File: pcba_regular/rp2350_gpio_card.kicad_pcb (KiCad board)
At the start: 4 copper layers, 26 x 30 mm, 37 parts, among them J1 Conn_01x10_Pin, J2 Conn_01x10_Pin, P1 USB_C_Plug_USB2.0, U1 RP2350_60QFN, U2 W25Q128JVS, U4 AP2127K-3.3, Y1 ABM8-272-T3

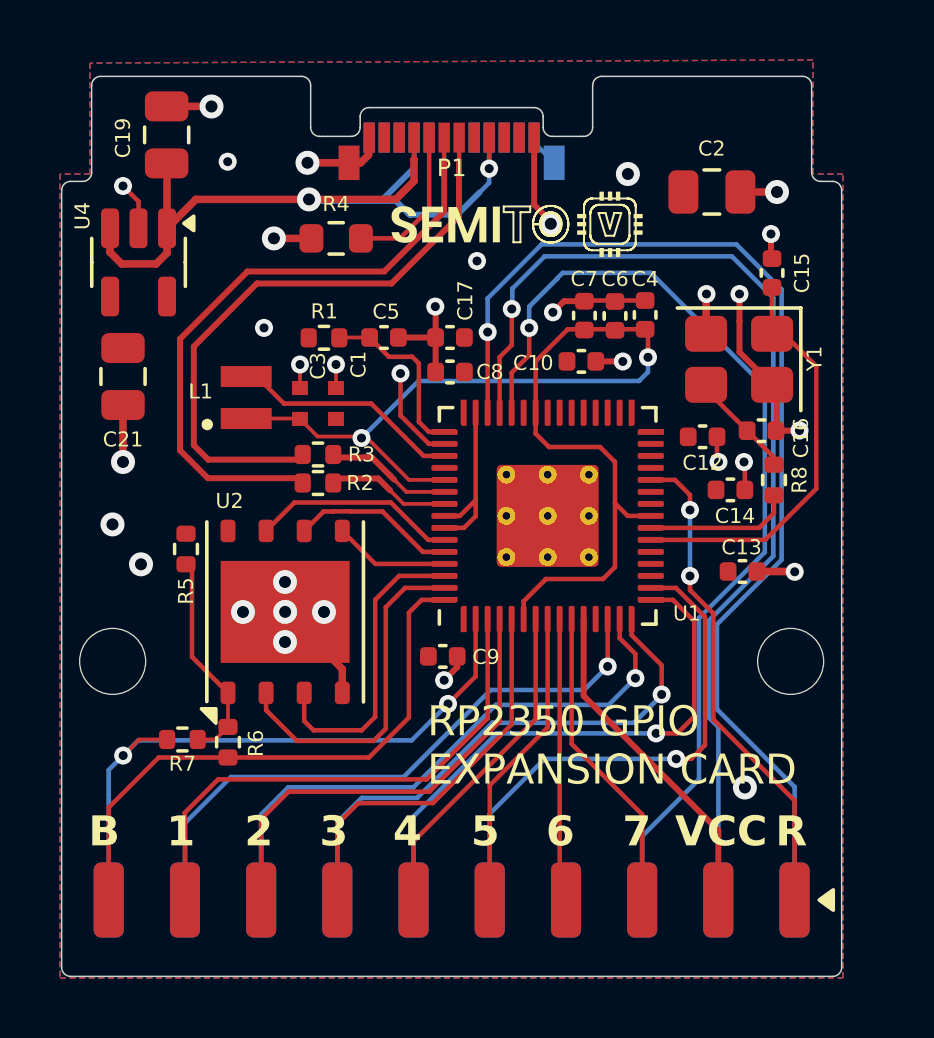
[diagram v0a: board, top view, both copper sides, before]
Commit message: optimized PCB layout
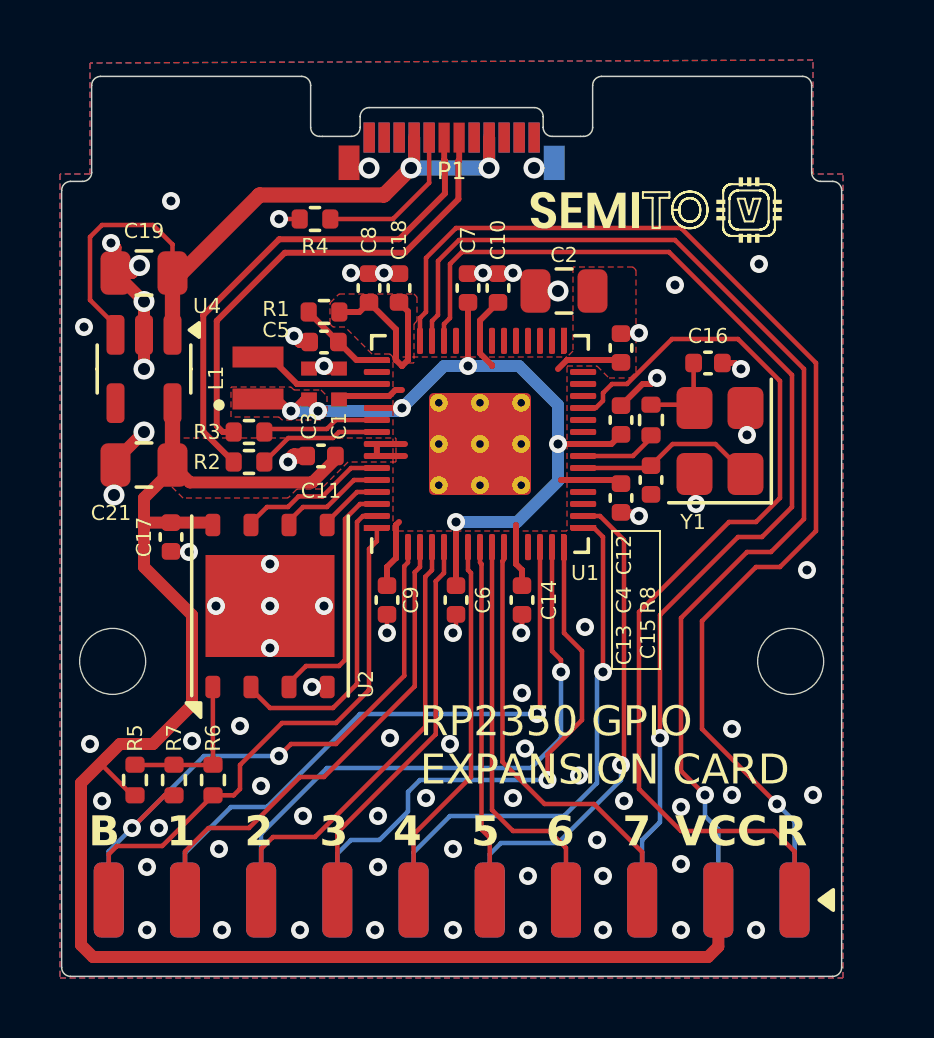
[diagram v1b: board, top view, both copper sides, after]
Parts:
- removed REF**: OSHW-Logo2_7.3x6mm_SilkScreen, Symbol:OSHW-Logo2_7.3x6mm_SilkScreen
- added C11: 100n, Capacitor_SMD:C_0402_1005Metric, F.Cu at (99.2, 64.8)
- added C18: 100n, Capacitor_SMD:C_0402_1005Metric, F.Cu at (101.8, 59.2)
- R4: footprint Resistor_SMD:R_0603_1608Metric -> Resistor_SMD:R_0402_1005Metric
- moved C17 11.4 mm to (94.2, 67.5), turned to -90 degrees
- moved C6 10.9 mm to (103.7, 69.6), turned to -90 degrees
- moved C15 7.99 mm to (110.2, 65.6), turned to -90 degrees
- moved R5 7.89 mm to (93.0, 75.6), turned to 90 degrees
- moved C14 7.86 mm to (105.9, 69.6), turned to -90 degrees
- moved C2 5.93 mm to (107.3, 59.3), turned to 180 degrees
- moved C13 4.73 mm to (109.2, 66.2), turned to -90 degrees
- moved C19 4.67 mm to (93.3, 58.7), turned to 180 degrees
- moved R8 4.56 mm to (110.2, 63.6)
- moved C12 4.02 mm to (109.2, 61.2), turned to 90 degrees
- moved C7 3.99 mm to (104.1, 59.2)
- moved C8 3.89 mm to (100.8, 59.2), turned to 90 degrees
- moved C10 3.70 mm to (105.1, 59.2), turned to 90 degrees
- moved C4 3.59 mm to (109.2, 63.6)
- moved U4 3.56 mm to (93.3, 61.9)
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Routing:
- net +3.3V: track 17.3 -> 76.5 mm
- net GND: track 44.3 -> 22.6 mm, vias 33 -> 76
- net /RUN: track 17.1 -> 32.0 mm, vias 2 -> 0
- net +1V1: track 38.1 -> 26.4 mm, vias 2 -> 6
- net /XIN: track 14.1 -> 6.16 mm
- net /USB_D-: track 20.5 -> 16.0 mm
- net /USB_D+: track 21.3 -> 16.9 mm
- net /VREG_LX: track 8.23 -> 4.34 mm
- net /GPIO7: track 10.9 -> 14.7 mm
- net /GPIO6: track 10.0 -> 13.5 mm
- net /VREG_AVDD: track 5.99 -> 2.94 mm
- net /GPIO27_ADC1: track 33.1 -> 35.9 mm
- net /XOUT: track 5.25 -> 2.60 mm
- net VBUS: track 28.1 -> 25.7 mm
- net /GPIO1: track 18.2 -> 16.3 mm
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- added copper zone on F.Cu, net +1V1
- added copper zone on F.Cu, net GND
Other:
- copper layers 4 -> 2
- board text added: "Designed by"
- board text added: "and jerrymk"
- board text added: "v1.4.0"
- board text removed: "Designed by:"
- board text removed: "v1.3.6"

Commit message: optimized back gnd plane
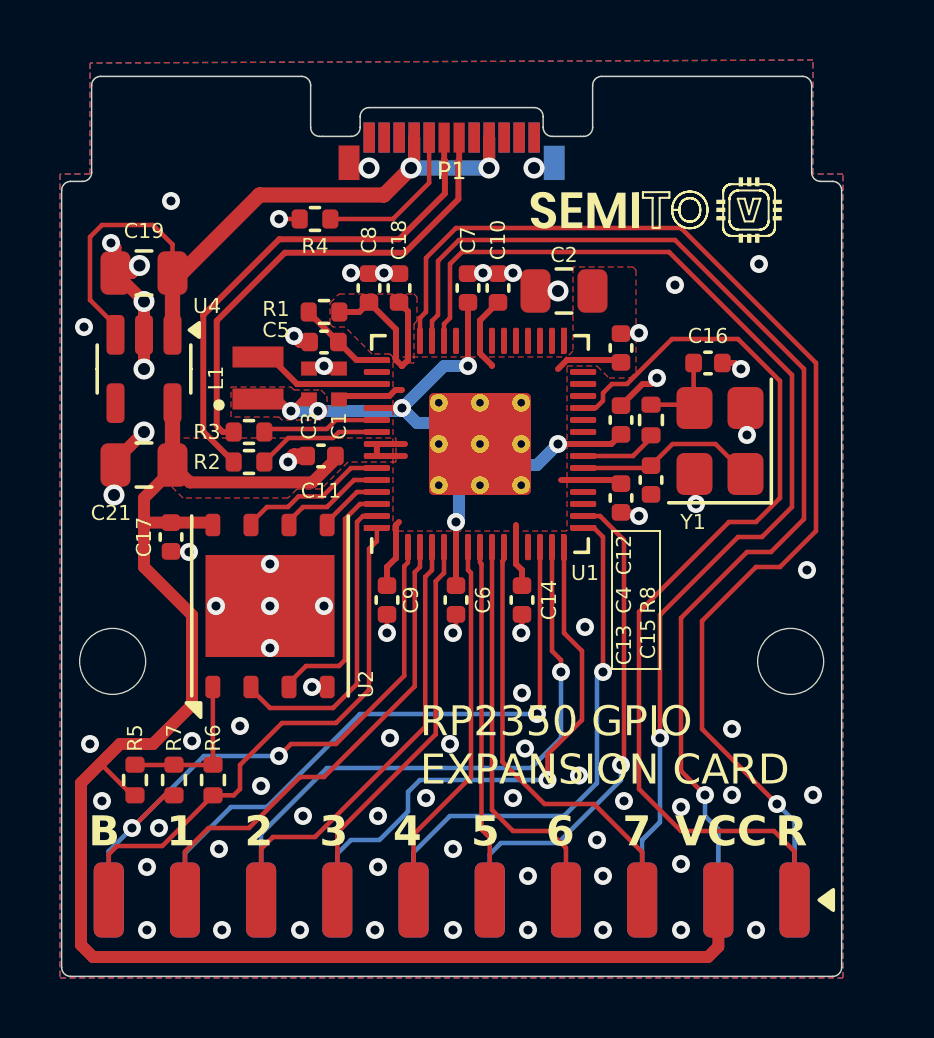
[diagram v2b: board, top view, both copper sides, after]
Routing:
- net +1V1: track 26.4 -> 25.2 mm
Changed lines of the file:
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@@
 	)
 	(segment
-		(start 107.1 65.638862)
-		(end 105.738862 67)
+		(start 98.2 63.3)
+		(end 99.1 63.3)
 		(width 0.4)
 		(layer "B.Cu")
@@
 	)
 	(segment
-		(start 98.2 63.3)
-		(end 99.1 63.3)
+		(start 103.781 64.131)
+		(end 103.8 64.15)
 		(width 0.4)
 		(layer "B.Cu")
@@
 	)
 	(segment
-		(start 105.8 61.8)
-		(end 107.1 63.1)
-		(width 0.4)
-		(layer "B.Cu")
-		(net 1)
-	)
-	(segment
-		(start 107.1 63.1)
-		(end 107.1 64.4)
-		(width 0.4)
-		(layer "B.Cu")
-		(net 1)
-	)
-	(segment
 		(start 103.3 61.8)
 		(end 101.9 63.2)
@@
 	)
 	(segment
-		(start 104.1 61.8)
-		(end 105.8 61.8)
+		(start 103.352724 63.7)
+		(end 103.781 64.128276)
 		(width 0.4)
 		(layer "B.Cu")
@@
 	)
 	(segment
-		(start 105.738862 67)
-		(end 103.7 67)
+		(start 103.8 64.15)
+		(end 103.8 65.1)
+		(width 0.4)
+		(layer "B.Cu")
+		(net 1)
+	)
+	(segment
+		(start 107.1 64.4)
+		(end 106.4 65.1)
+		(width 0.4)
+		(layer "B.Cu")
+		(net 1)
+	)
+	(segment
+		(start 101.9 63.2)
+		(end 102.4 63.7)
+		(width 0.4)
+		(layer "B.Cu")
+		(net 1)
+	)
+	(segment
+		(start 102.4 63.7)
+		(end 103.352724 63.7)
+		(width 0.4)
+		(layer "B.Cu")
+		(net 1)
+	)
+	(segment
+		(start 106.4 65.1)
+		(end 103.8 65.1)
+		(width 0.4)
+		(layer "B.Cu")
+		(net 1)
+	)
+	(segment
+		(start 103.781 64.128276)
+		(end 103.781 64.131)
 		(width 0.4)
 		(layer "B.Cu")
@@
 	)
 	(segment
-		(start 107.1 64.4)
-		(end 107.1 65.638862)
+		(start 103.8 65.1)
+		(end 103.8 66.9)
 		(width 0.4)
 		(layer "B.Cu")
+		(net 1)
+	)
+	(segment
+		(start 103.8 66.9)
+		(end 103.7 67)
+		(width 0.4)
+		(layer "B.Cu")

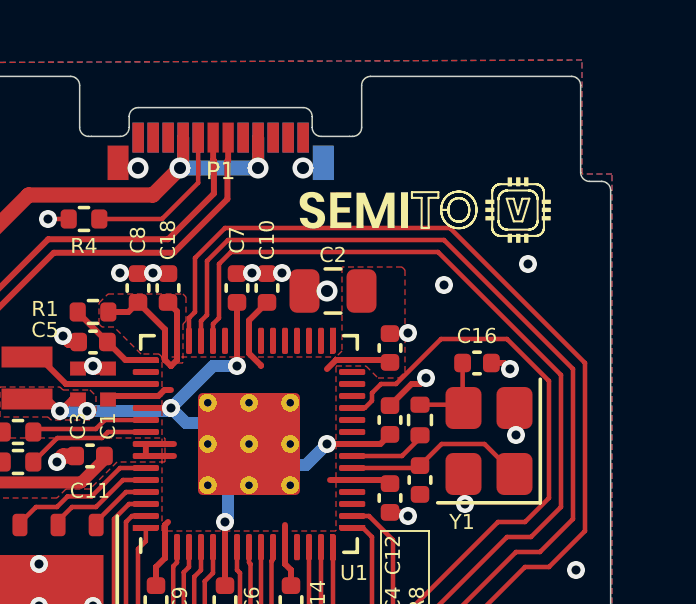
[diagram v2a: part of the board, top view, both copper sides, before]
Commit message: added open hardware graphics back
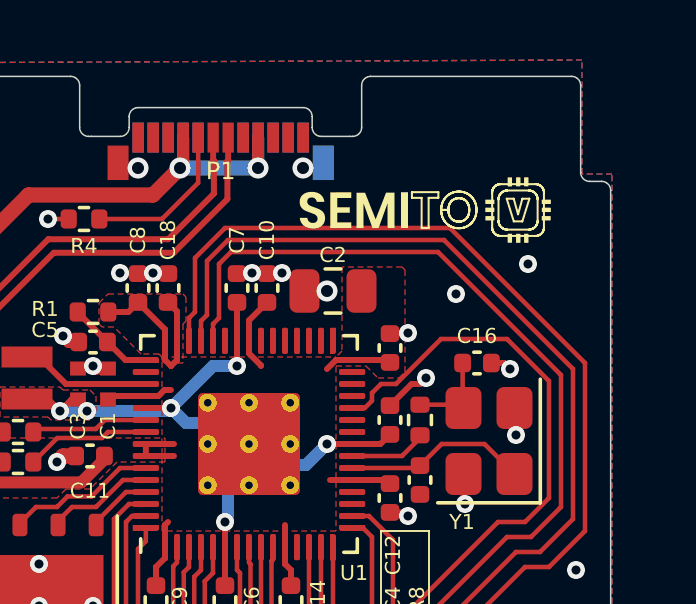
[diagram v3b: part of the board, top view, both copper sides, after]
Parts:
- added REF**: OSHW-Logo2_7.3x6mm_SilkScreen, Symbol:OSHW-Logo2_7.3x6mm_SilkScreen, B.Cu at (112.4, 58.0)

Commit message: clean up
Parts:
- moved C11 0.10 mm to (99.1, 64.8)
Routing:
- net +1V1: track 25.2 -> 26.4 mm
- net +3.3V: track 76.5 -> 75.7 mm
- net /VREG_LX: track 4.34 -> 3.65 mm

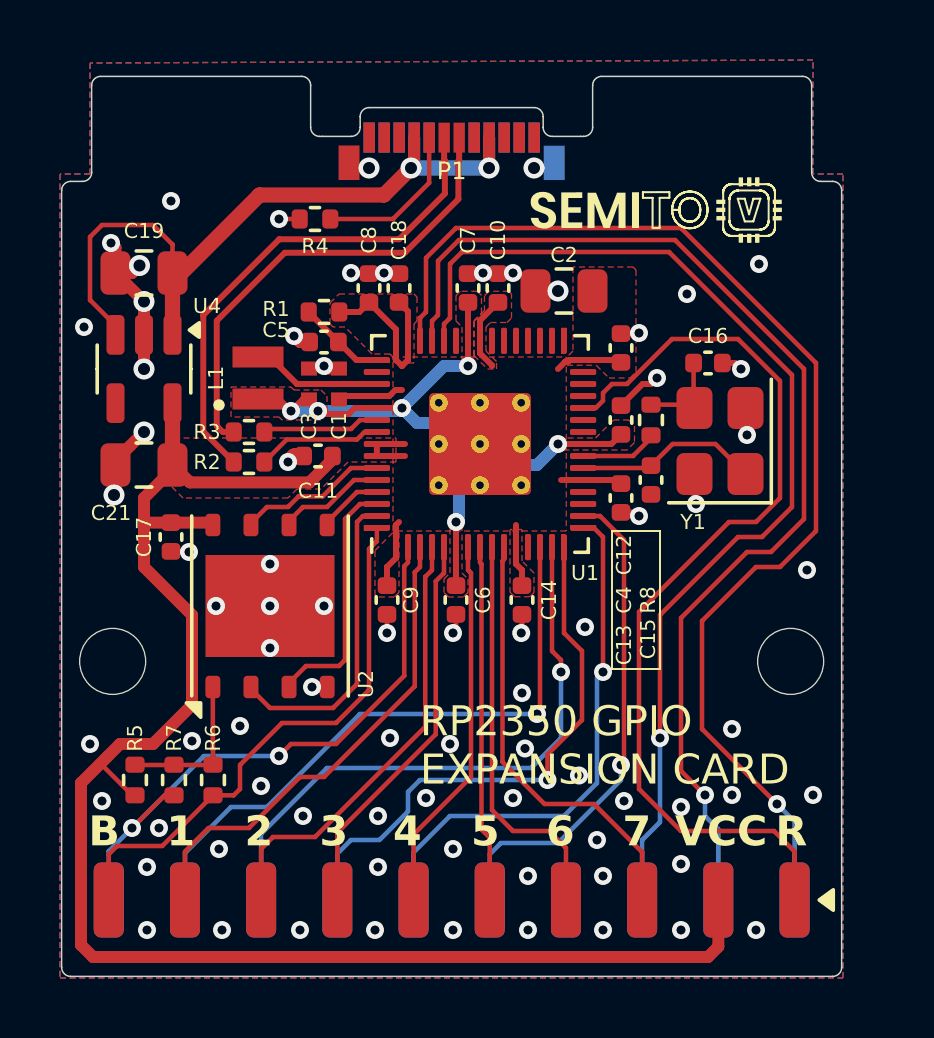
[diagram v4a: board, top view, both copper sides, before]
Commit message: fix DRC errors and increase clearances
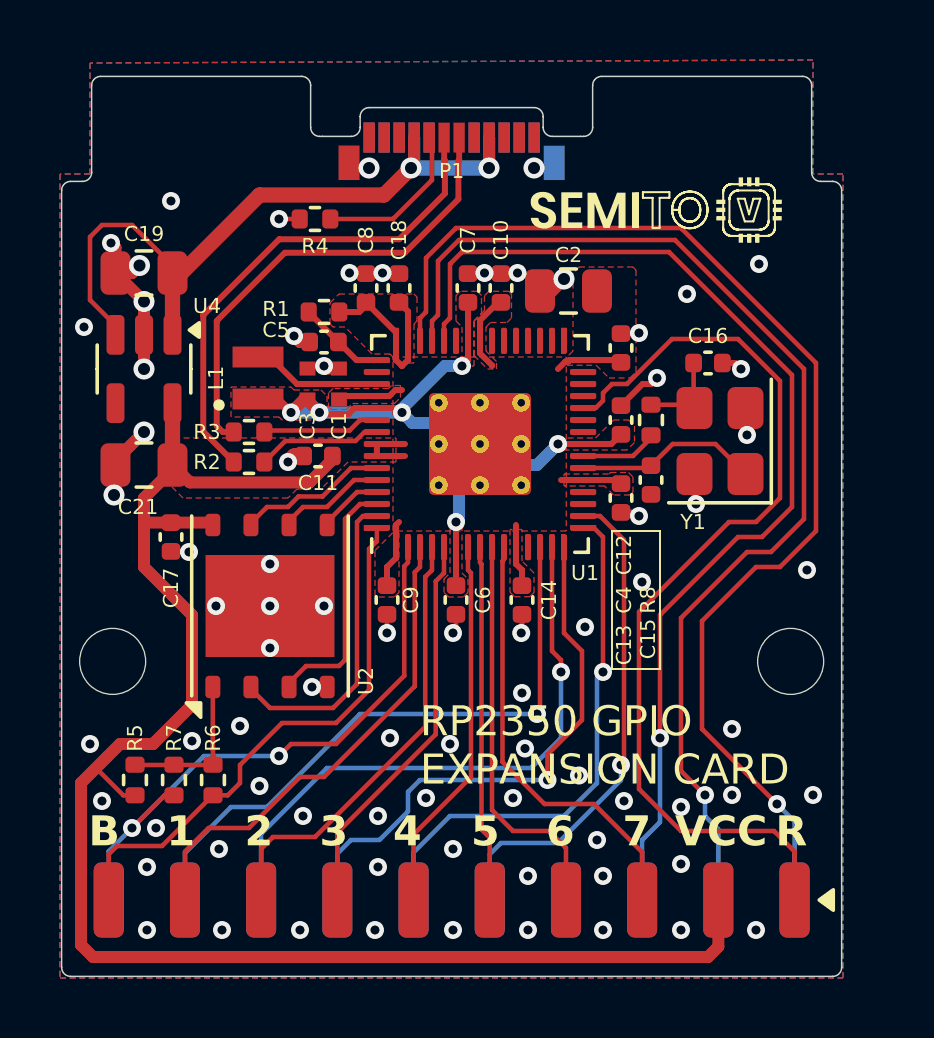
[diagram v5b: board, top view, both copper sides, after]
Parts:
- moved C2 0.15 mm to (107.5, 59.3)
- moved C10 0.10 mm to (105.2, 59.2)
- moved C8 0.10 mm to (100.7, 59.2)
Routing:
- net VBUS: track 25.3 -> 24.7 mm
- net GND: track 22.2 -> 22.6 mm, vias 76 -> 77
